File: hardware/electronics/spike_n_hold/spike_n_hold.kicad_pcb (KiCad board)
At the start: 2 copper layers, 63 x 110.5 mm, 54 parts, among them J1 input_trigger_2, J2 input_trigger_1, J3 to_solenoid_2, J4 to_solenoid_1, J9 Barrel_Jack_MountingPin, Q1 MJH11021G, Q2 MJH11021G, Q3 MPSA42, Q4 MPSA42, Q5 MPSA42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

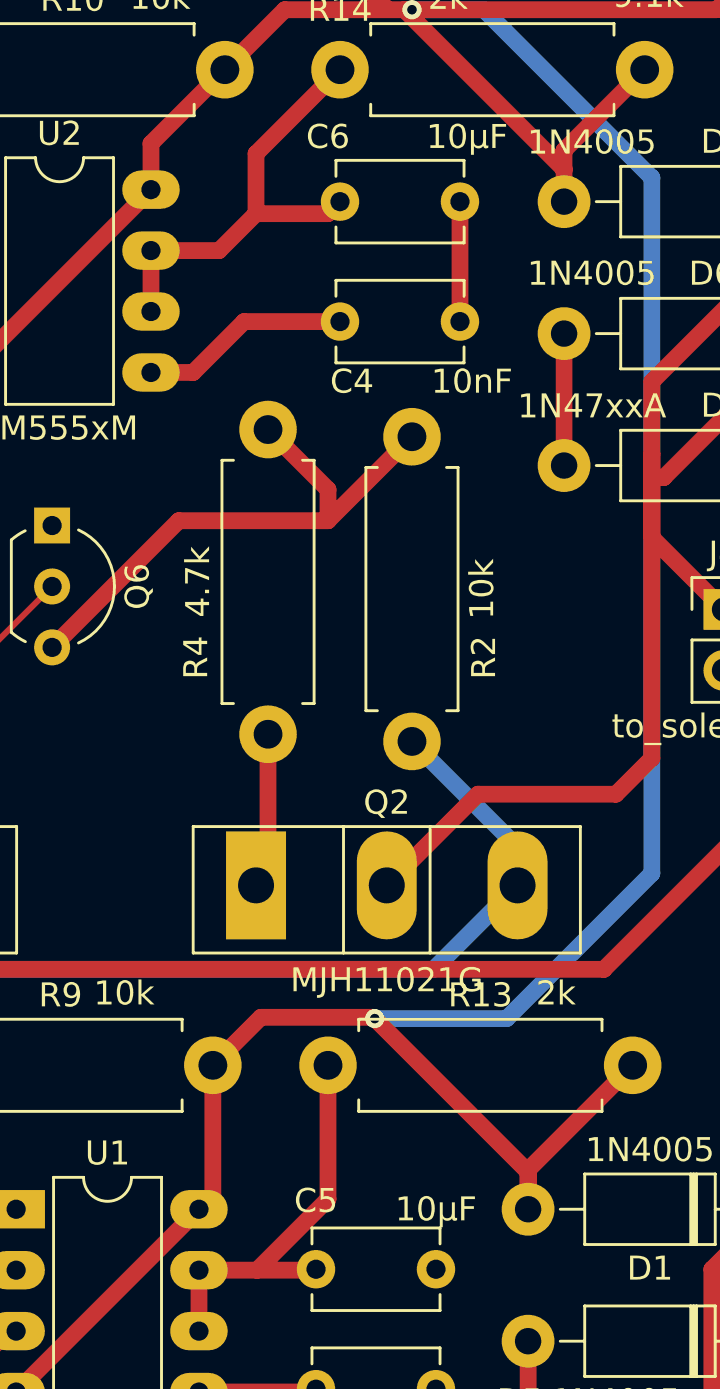
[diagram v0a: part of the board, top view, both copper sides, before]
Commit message: remove excessive track on board (two ground tracks going to same place), add + sign on polar capacitors, add 3D models for connectors
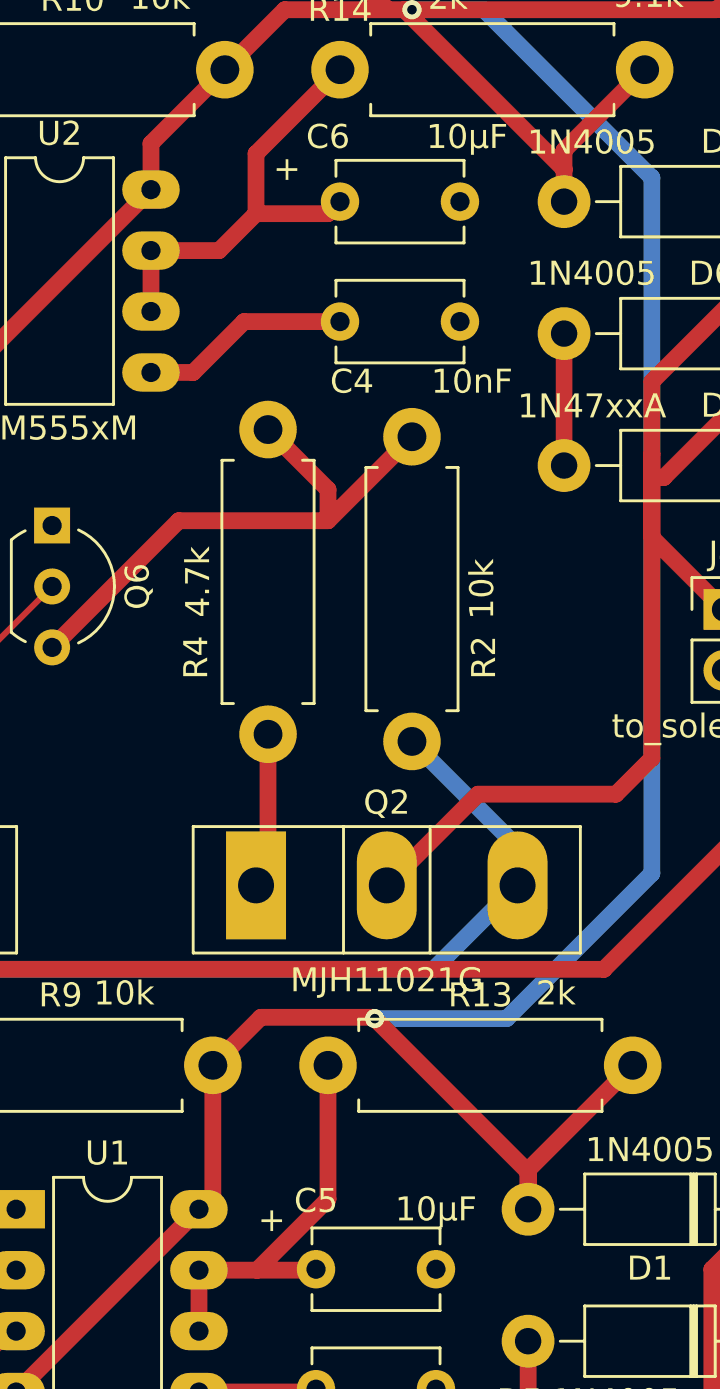
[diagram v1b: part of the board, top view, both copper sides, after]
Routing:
- net GND: track 5.00 -> 0.00 mm
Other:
- board text added: "+"
